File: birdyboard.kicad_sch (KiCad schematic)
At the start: 37 parts, among them J1 24V Input Screw Terminal, J10 JST-PH StepMotor Conn, J11 TBP02R2-381-04BE, J12 AS5047_Adapter_Board_Connector, J13 AS5047_Adapter_Board_Connector, J14 AS5047_Adapter_Board_Connector, J15 AS5047_Adapter_Board_Connector, J2 24V Input Screw Terminal, J3 24V Input Screw Terminal, J4 JST-PH StepMotor Conn, J5 JST-PH StepMotor Conn, J6 JST-PH StepMotor Conn, J7 TBP02R2-381-04BE, J8 TBP02R2-381-04BE, J9 TBP02R2-381-04BE, U3 Pico, U6 SN74CBT3253 MUX/DEMUX, U7 AZ1117CH-3_3TRG1

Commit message: Update Schematic Labels
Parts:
- gave numbers to parts that had none: 4
- renumbered J11 to J10, J10 to J3, U3 to U0, PS1 to U5, U7 to U6
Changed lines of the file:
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@@
   (symbol (lib_id "birdyboard_library:TMC2209_SILENTSTEPSTICK") (at 123.19 39.37 0) (unit 1)
     (in_bom yes) (on_board yes) (fields_autoplaced)
-    (property "Reference" "U?" (id 0) (at 110.49 20.32 0)
-      (effects (font (size 1.27 1.27)) (justify left bottom))
-    )
-    (property "Value" "TMC2209_SILENTSTEPSTICK" (id 1) (at 110.49 62.23 0)
-      (effects (font (size 1.27 1.27)) (justify left bottom))
-    )
+    (property "Reference" "U2" (id 0) (at 123.19 16.51 0))
+    (property "Value" "TMC2209_SILENTSTEPSTICK" (id 1) (at 123.19 19.05 0))
     (property "Footprint" "MODULE_TMC2208_SILENTSTEPSTICK" (id 2) (at 123.19 39.37 0)
       (effects (font (size 1.27 1.27)) (justify left bottom) hide)
@@
   (symbol (lib_id "birdyboard_library:TMC2209_SILENTSTEPSTICK") (at 43.815 172.085 0) (unit 1)
     (in_bom yes) (on_board yes) (fields_autoplaced)
-    (property "Reference" "U?" (id 0) (at 31.115 153.035 0)
-      (effects (font (size 1.27 1.27)) (justify left bottom))
-    )
-    (property "Value" "TMC2209_SILENTSTEPSTICK" (id 1) (at 31.115 194.945 0)
-      (effects (font (size 1.27 1.27)) (justify left bottom))
-    )
+    (property "Reference" "U3" (id 0) (at 43.815 148.59 0))
+    (property "Value" "TMC2209_SILENTSTEPSTICK" (id 1) (at 43.815 151.13 0))
     (property "Footprint" "MODULE_TMC2208_SILENTSTEPSTICK" (id 2) (at 43.815 172.085 0)
       (effects (font (size 1.27 1.27)) (justify left bottom) hide)
@@
   (symbol (lib_id "birdyboard_library:Pico") (at 102.87 106.68 0) (unit 1)
     (in_bom yes) (on_board yes) (fields_autoplaced)
-    (property "Reference" "U3" (id 0) (at 102.87 74.93 0))
+    (property "Reference" "U0" (id 0) (at 102.87 74.93 0))
     (property "Value" "Pico" (id 1) (at 102.87 77.47 0))
     (property "Footprint" "MCU_RaspberryPi_and_Boards:RPi_Pico_SMD_TH" (id 2) (at 102.87 106.68 90)
@@
   (symbol (lib_id "birdyboard_library:TBP02R2-381-04BE") (at 42.545 8.89 0) (unit 1)
     (in_bom yes) (on_board yes) (fields_autoplaced)
-    (property "Reference" "J11" (id 0) (at 49.53 6.3499 0)
+    (property "Reference" "J10" (id 0) (at 49.53 6.3499 0)
       (effects (font (size 1.27 1.27)) (justify left))
     )
@@
   (symbol (lib_id "birdyboard_library:K7805-3AR3") (at 202.565 60.96 0) (unit 1)
     (in_bom yes) (on_board yes) (fields_autoplaced)
-    (property "Reference" "PS1" (id 0) (at 202.565 45.72 0))
+    (property "Reference" "U5" (id 0) (at 202.565 45.72 0))
     (property "Value" "K7805-3AR3" (id 1) (at 202.565 48.26 0))
     (property "Footprint" "birdyboard:CONV_K7805-3AR3" (id 2) (at 202.565 50.8 0))
@@
   (symbol (lib_id "dk_PMIC-Voltage-Regulators-Linear:AZ1117CH-3_3TRG1") (at 201.93 24.765 0) (unit 1)
     (in_bom yes) (on_board yes) (fields_autoplaced)
-    (property "Reference" "U7" (id 0) (at 203.2 16.51 0)
+    (property "Reference" "U6" (id 0) (at 203.2 16.51 0)
       (effects (font (size 1.524 1.524)))
     )
@@
   (symbol (lib_id "Connector:Conn_01x04_Female") (at 163.195 171.45 0) (unit 1)
     (in_bom yes) (on_board yes)
-    (property "Reference" "J10" (id 0) (at 167.005 176.53 0)
+    (property "Reference" "J3" (id 0) (at 167.005 176.53 0)
       (effects (font (size 1.27 1.27)) (justify left))
     )
@@
   (symbol (lib_id "birdyboard_library:TMC2209_SILENTSTEPSTICK") (at 40.64 37.465 0) (unit 1)
     (in_bom yes) (on_board yes) (fields_autoplaced)
-    (property "Reference" "U?" (id 0) (at 27.94 18.415 0)
-      (effects (font (size 1.27 1.27)) (justify left bottom))
-    )
-    (property "Value" "TMC2209_SILENTSTEPSTICK" (id 1) (at 27.94 60.325 0)
-      (effects (font (size 1.27 1.27)) (justify left bottom))
-    )
+    (property "Reference" "U1" (id 0) (at 40.64 13.97 0))
+    (property "Value" "TMC2209_SILENTSTEPSTICK" (id 1) (at 40.64 16.51 0))
     (property "Footprint" "MODULE_TMC2208_SILENTSTEPSTICK" (id 2) (at 40.64 37.465 0)
       (effects (font (size 1.27 1.27)) (justify left bottom) hide)
@@
   (symbol (lib_id "birdyboard_library:TMC2209_SILENTSTEPSTICK") (at 132.715 171.45 0) (unit 1)
     (in_bom yes) (on_board yes) (fields_autoplaced)
-    (property "Reference" "U?" (id 0) (at 120.015 152.4 0)
-      (effects (font (size 1.27 1.27)) (justify left bottom))
-    )
-    (property "Value" "TMC2209_SILENTSTEPSTICK" (id 1) (at 120.015 194.31 0)
-      (effects (font (size 1.27 1.27)) (justify left bottom))
-    )
+    (property "Reference" "U4" (id 0) (at 132.715 148.59 0))
+    (property "Value" "TMC2209_SILENTSTEPSTICK" (id 1) (at 132.715 151.13 0))
     (property "Footprint" "MODULE_TMC2208_SILENTSTEPSTICK" (id 2) (at 132.715 171.45 0)
       (effects (font (size 1.27 1.27)) (justify left bottom) hide)
@@
       (reference "J2") (unit 1) (value "24V Input Screw Terminal") (footprint "birdyboard:CUI_TBP01R2-508-02BE")
     )
+    (path "/acf46d64-7022-46aa-a07f-964eb7e04114"
+      (reference "J3") (unit 1) (value "JST-PH StepMotor Conn") (footprint "Connector_JST:JST_XH_B4B-XH-A_1x04_P2.50mm_Vertical")
+    )
     (path "/f5df09cc-e7d8-40ed-81dc-431146d8ff35"
       (reference "J3") (unit 1) (value "24V Input Screw Terminal") (footprint "birdyboard:CUI_TBP01R2-508-02BE")
@@
       (reference "J9") (unit 1) (value "TBP02R2-381-04BE") (footprint "birdyboard:CUI_TBP02R2-381-04BE")
     )
-    (path "/acf46d64-7022-46aa-a07f-964eb7e04114"
-      (reference "J10") (unit 1) (value "JST-PH StepMotor Conn") (footprint "Connector_JST:JST_XH_B4B-XH-A_1x04_P2.50mm_Vertical")
-    )
     (path "/6c972ed1-f9ff-48f3-b910-a3798639139c"
-      (reference "J11") (unit 1) (value "TBP02R2-381-04BE") (footprint "birdyboard:CUI_TBP02R2-381-04BE")
+      (reference "J10") (unit 1) (value "TBP02R2-381-04BE") (footprint "birdyboard:CUI_TBP02R2-381-04BE")
     )
     (path "/3bced514-7c6a-4929-a2f4-97c9dfd34def"
@@
       (reference "JP?") (unit 1) (value "SolderJumper_3_Bridged12") (footprint "")
     )
-    (path "/8ce54405-acb6-4808-8ae9-05b938524726"
-      (reference "PS1") (unit 1) (value "K7805-3AR3") (footprint "birdyboard:CONV_K7805-3AR3")
-    )
     (path "/1383c2e0-9014-4320-87a3-9259c9c126ad"
       (reference "R?") (unit 1) (value "R") (footprint "")
@@
     )
     (path "/5c28b9b9-20a8-48b6-ba53-d717d342083f"
-      (reference "U3") (unit 1) (value "Pico") (footprint "MCU_RaspberryPi_and_Boards:RPi_Pico_SMD_TH")
+      (reference "U0") (unit 1) (value "Pico") (footprint "MCU_RaspberryPi_and_Boards:RPi_Pico_SMD_TH")
+    )
+    (path "/c5ba89e5-abf6-44af-8c5f-769135662d59"
+      (reference "U1") (unit 1) (value "TMC2209_SILENTSTEPSTICK") (footprint "MODULE_TMC2208_SILENTSTEPSTICK")
+    )
+    (path "/1b7241dd-50c0-4ea4-b9e4-398fecb92930"
+      (reference "U2") (unit 1) (value "TMC2209_SILENTSTEPSTICK") (footprint "MODULE_TMC2208_SILENTSTEPSTICK")
+    )
+    (path "/344822b8-0c78-4832-98d5-254b8b20341d"
+      (reference "U3") (unit 1) (value "TMC2209_SILENTSTEPSTICK") (footprint "MODULE_TMC2208_SILENTSTEPSTICK")
+    )
+    (path "/f64ad3d7-b9b7-403e-af6d-671c637d8a55"
+      (reference "U4") (unit 1) (value "TMC2209_SILENTSTEPSTICK") (footprint "MODULE_TMC2208_SILENTSTEPSTICK")
+    )
+    (path "/8ce54405-acb6-4808-8ae9-05b938524726"
+      (reference "U5") (unit 1) (value "K7805-3AR3") (footprint "birdyboard:CONV_K7805-3AR3")
     )
     (path "/71a1570f-8306-437b-8e8c-580fc1ad37d6"
@@
     )
     (path "/a15739ab-9211-4aeb-9603-bc7b827421d7"
-      (reference "U7") (unit 1) (value "AZ1117CH-3_3TRG1") (footprint "digikey-footprints:SOT-223")
-    )
-    (path "/1b7241dd-50c0-4ea4-b9e4-398fecb92930"
-      (reference "U?") (unit 1) (value "TMC2209_SILENTSTEPSTICK") (footprint "MODULE_TMC2208_SILENTSTEPSTICK")
-    )
-    (path "/344822b8-0c78-4832-98d5-254b8b20341d"
-      (reference "U?") (unit 1) (value "TMC2209_SILENTSTEPSTICK") (footprint "MODULE_TMC2208_SILENTSTEPSTICK")
-    )
-    (path "/c5ba89e5-abf6-44af-8c5f-769135662d59"
-      (reference "U?") (unit 1) (value "TMC2209_SILENTSTEPSTICK") (footprint "MODULE_TMC2208_SILENTSTEPSTICK")
-    )
-    (path "/f64ad3d7-b9b7-403e-af6d-671c637d8a55"
-      (reference "U?") (unit 1) (value "TMC2209_SILENTSTEPSTICK") (footprint "MODULE_TMC2208_SILENTSTEPSTICK")
-    )
-  )
+      (reference "U6") (unit 1) (value "AZ1117CH-3_3TRG1") (footprint "digikey-footprints:SOT-223")
+    )
+  )

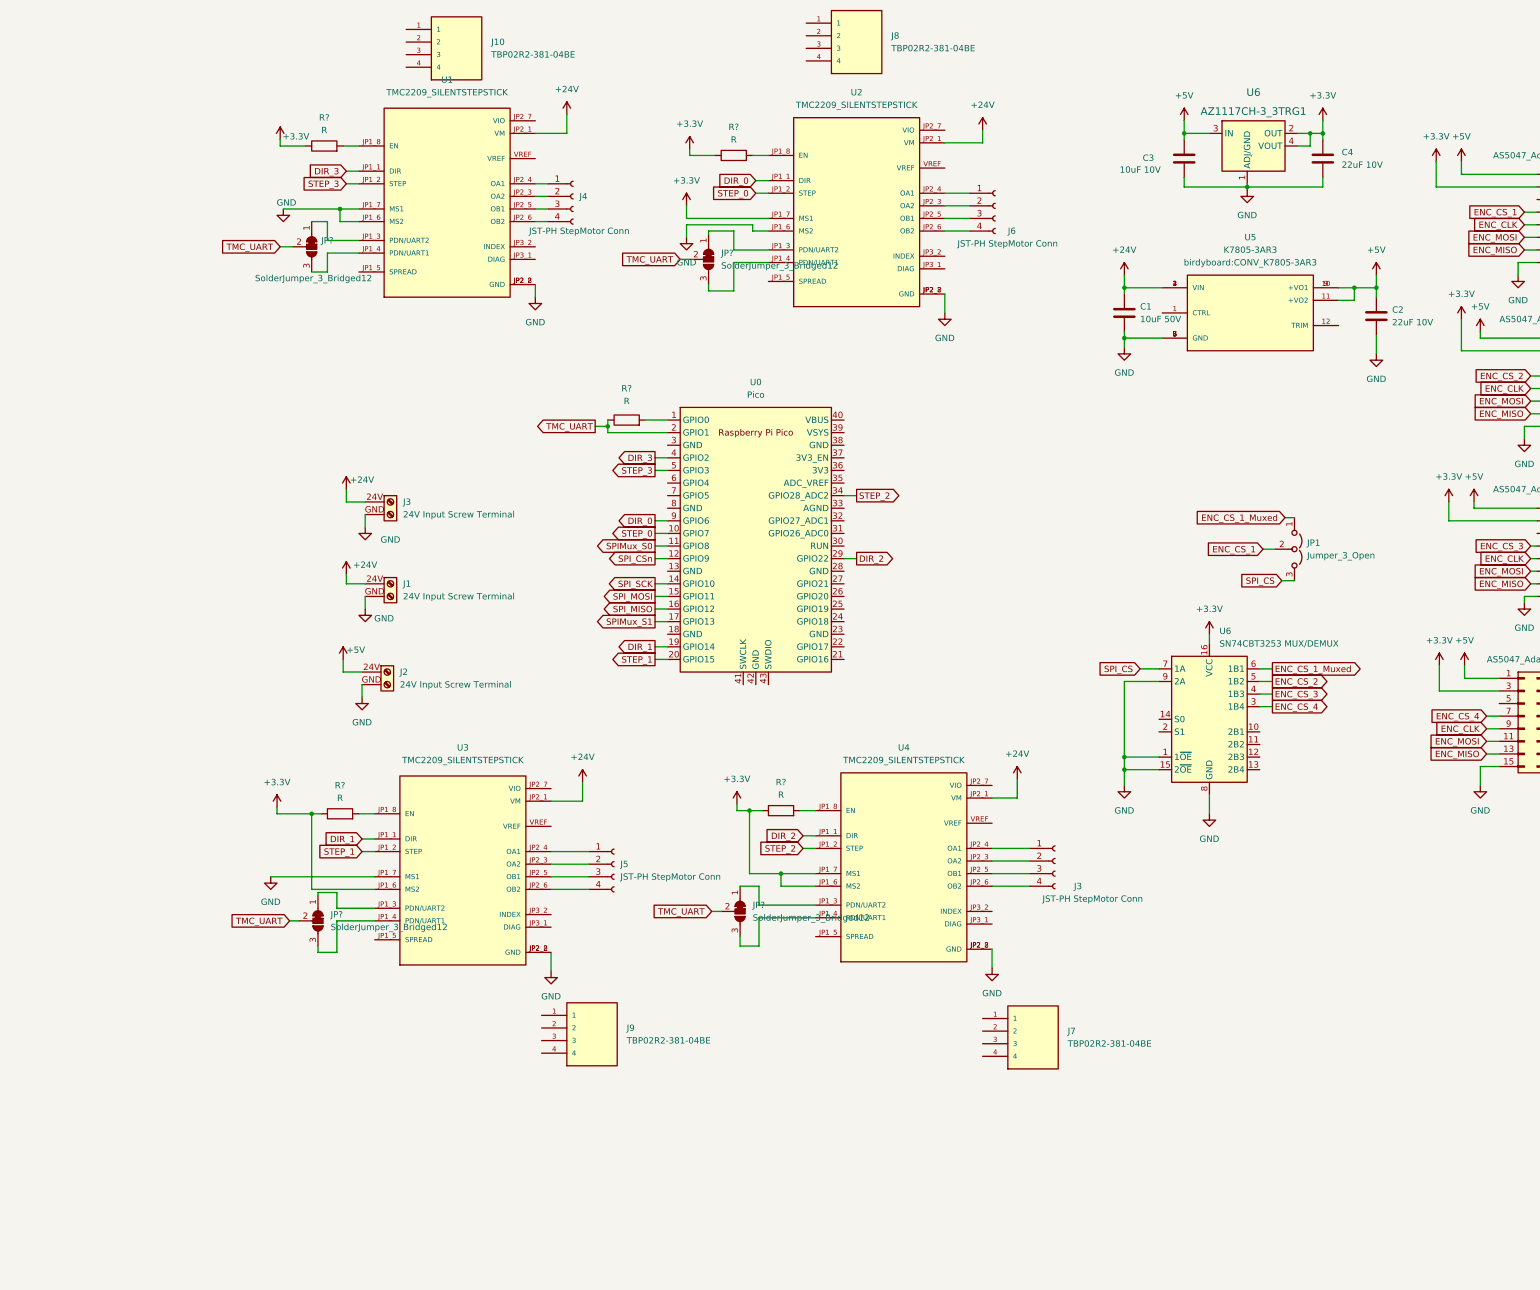
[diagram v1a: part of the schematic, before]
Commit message: Adds 40-pin header, cleans up stepper connections, add VIO connections for TMC, hooks up RP-PICO Power
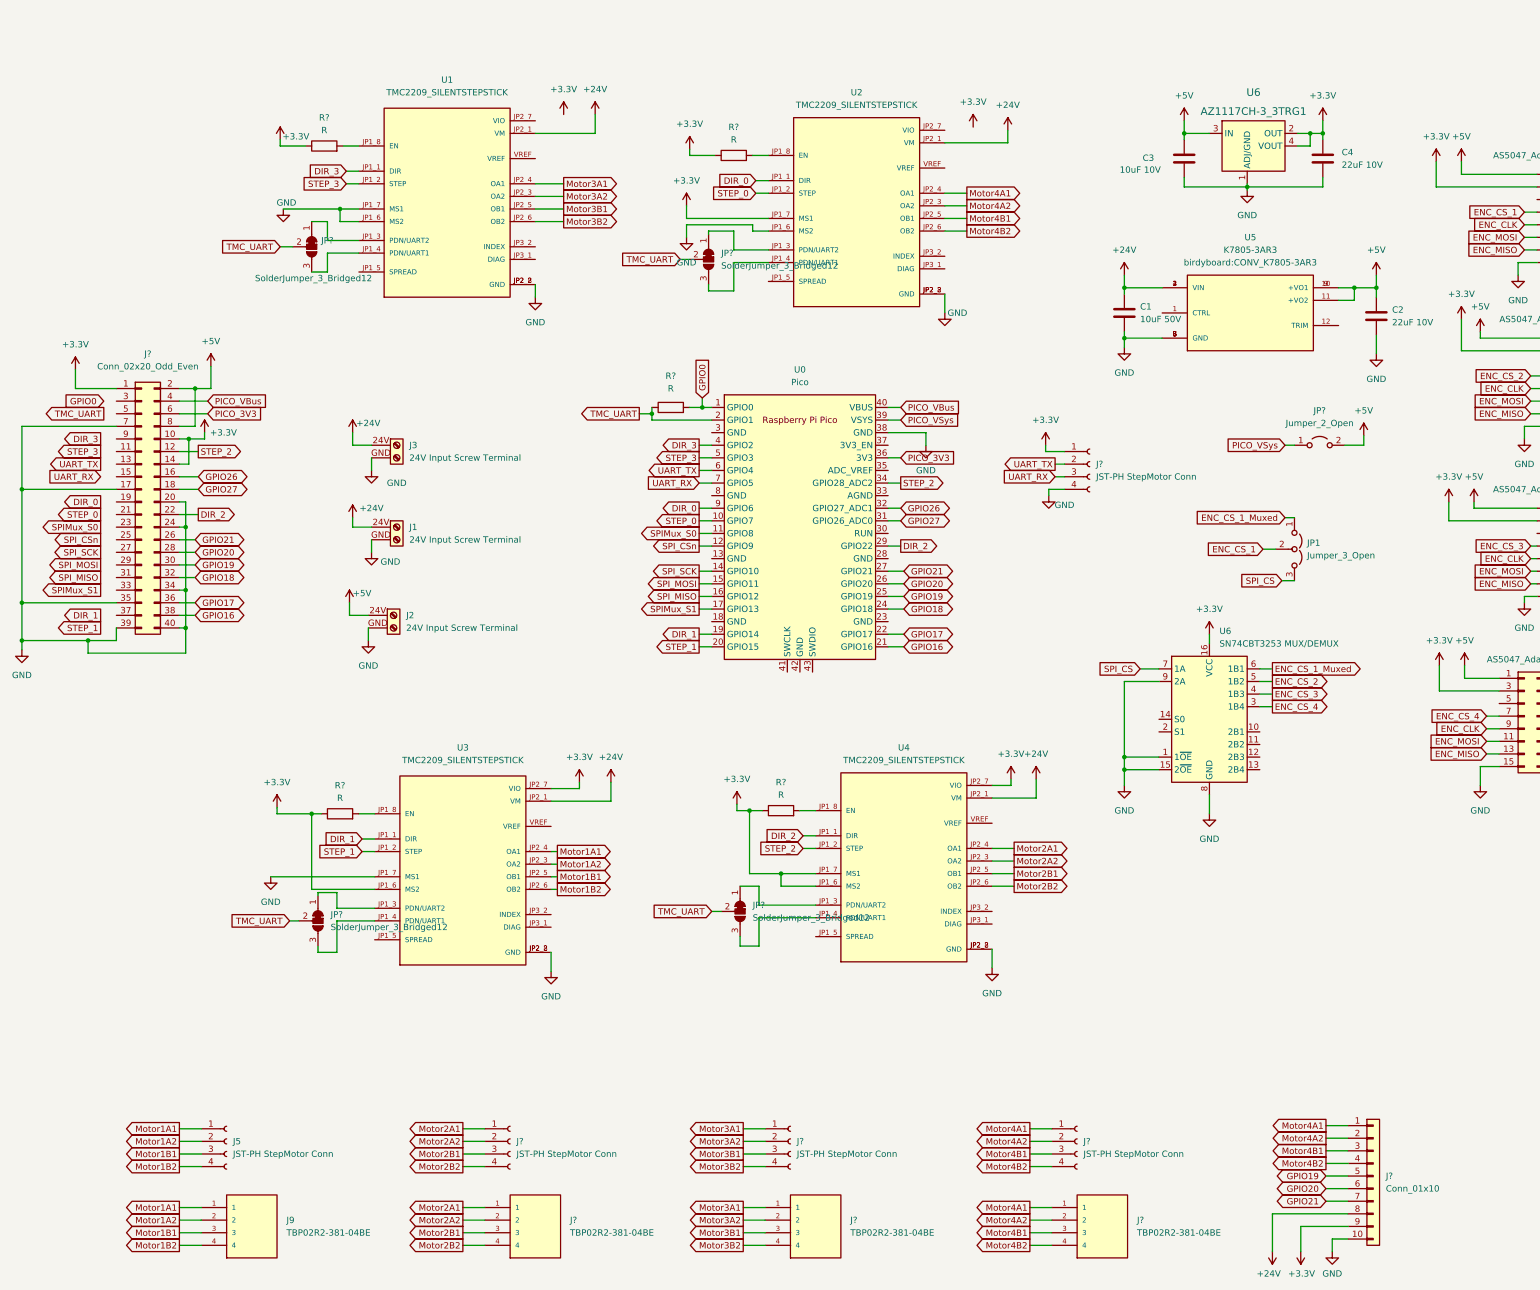
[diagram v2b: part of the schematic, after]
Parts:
- removed J10, J7, J8: TBP02R2-381-04BE, birdyboard:CUI_TBP02R2-381-04BE, symbol birdyboard_library:TBP02R2-381-04BE
- removed J3, J4, J6: JST-PH StepMotor Conn, Connector_JST:JST_XH_B4B-XH-A_1x04_P2.50mm_Vertical, symbol Connector:Conn_01x04_Female
- added J? (x4): JST-PH StepMotor Conn, Connector_JST:JST_XH_B4B-XH-A_1x04_P2.50mm_Vertical, symbol Connector:Conn_01x04_Female
- added J? (x3): TBP02R2-381-04BE, birdyboard:CUI_TBP02R2-381-04BE, symbol birdyboard_library:TBP02R2-381-04BE
- added J?: Conn_02x20_Odd_Even, Connector_PinHeader_2.54mm:PinHeader_2x20_P2.54mm_Vertical, symbol Connector_Generic:Conn_02x20_Odd_Even
- added J?: Conn_01x10, symbol Connector_Generic:Conn_01x10
- added JP?: Jumper_2_Open, symbol Jumper:Jumper_2_Open
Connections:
- net +24V: now also J?.8 (Pin_8)
- net +3.3V: now also J?.1 (Pin_1), J?.1 (Pin_1), J?.10 (Pin_10), J?.14 (Pin_14), J?.9 (Pin_9)
- net +3V3: now also U3.JP2_7 (VIO), U4.JP2_7 (VIO)
- net +5V: now also J?.2 (Pin_2), J?.8 (Pin_8), JP?.2 (B)
- net DIR_2: now also J?.22 (Pin_22)
- net GND: now also U0.38 (GND), J?.10 (Pin_10), J?.17 (Pin_17), J?.20 (Pin_20), J?.24 (Pin_24), J?.34 (Pin_34), J?.35 (Pin_35), J?.39 (Pin_39), J?.4 (Pin_4), J?.40 (Pin_40), J?.7 (Pin_7)
- net STEP_2: now also J?.12 (Pin_12)
- net GPIO0: now reaches R?.2, U0.1 (GPIO0)
- net Motor4A2: now reaches U2.JP2_3 (OA2)
- net Motor4A2: now also J?.2, J?.2 (Pin_2), J?.2 (Pin_2)
- net Motor4A1: now reaches U2.JP2_4 (OA1)
- net Motor4A1: now also J?.1, J?.1 (Pin_1), J?.1 (Pin_1)
- net Motor4B1: now reaches U2.JP2_5 (OB1)
- net Motor4B1: now also J?.3, J?.3 (Pin_3), J?.3 (Pin_3)
- net Motor4B2: now reaches U2.JP2_6 (OB2)
- net Motor4B2: now also J?.4, J?.4 (Pin_4), J?.4 (Pin_4)
- net Motor1A2: now reaches J5.2 (Pin_2), U3.JP2_3 (OA2)
- net Motor1A2: now also J9.2
- net Motor1A1: now reaches J5.1 (Pin_1), U3.JP2_4 (OA1)
- net Motor1A1: now also J9.1
- net Motor1B1: now reaches J5.3 (Pin_3), U3.JP2_5 (OB1)
- net Motor1B1: now also J9.3
- net Motor1B2: now reaches J5.4 (Pin_4), U3.JP2_6 (OB2)
- net Motor1B2: now also J9.4
- net GPIO16: now reaches U0.21 (GPIO16)
- net GPIO16: now also J?.38 (Pin_38)
- net GPIO17: now reaches U0.22 (GPIO17)
- net GPIO17: now also J?.36 (Pin_36)
- net GPIO18: now reaches U0.24 (GPIO18)
- net GPIO18: now also J?.32 (Pin_32)
- net GPIO19: now reaches U0.25 (GPIO19)
- net GPIO19: now also J?.30 (Pin_30), J?.5 (Pin_5)
- net GPIO20: now reaches U0.26 (GPIO20)
- net GPIO20: now also J?.28 (Pin_28), J?.6 (Pin_6)
- net GPIO21: now reaches U0.27 (GPIO21)
- net GPIO21: now also J?.26 (Pin_26), J?.7 (Pin_7)
- net GPIO27: now reaches U0.31 (GPIO26_ADC0)
- net GPIO27: now also J?.18 (Pin_18)
- net GPIO26: now reaches U0.32 (GPIO27_ADC1)
- net GPIO26: now also J?.16 (Pin_16)
- net PICO_3V3: now reaches U0.36 (3V3)
- net PICO_3V3: now also J?.6 (Pin_6)
- net PICO_VSys: now reaches U0.39 (VSYS)
- net PICO_VSys: now also JP?.1 (A)
- net PICO_VBus: now reaches U0.40 (VBUS)
- net PICO_VBus: now also J?.4 (Pin_4)
- net UART_TX: now reaches U0.6 (GPIO4)
- net UART_TX: now also J?.2 (Pin_2)
- net UART_RX: now reaches U0.7 (GPIO5)
- net UART_RX: now also J?.3 (Pin_3)
- net Motor3A1: now reaches U1.JP2_4 (OA1)
- net Motor3A1: now also J?.1, J?.1 (Pin_1)
- net Motor3A2: now reaches U1.JP2_3 (OA2)
- net Motor3A2: now also J?.2, J?.2 (Pin_2)
- net Motor3B1: now reaches U1.JP2_5 (OB1)
- net Motor3B1: now also J?.3, J?.3 (Pin_3)
- net Motor3B2: now reaches U1.JP2_6 (OB2)
- net Motor3B2: now also J?.4, J?.4 (Pin_4)
- net Motor2A1: now reaches U4.JP2_4 (OA1)
- net Motor2A1: now also J?.1, J?.1 (Pin_1)
- net Motor2A2: now reaches U4.JP2_3 (OA2)
- net Motor2A2: now also J?.2, J?.2 (Pin_2)
- net Motor2B1: now reaches U4.JP2_5 (OB1)
- net Motor2B1: now also J?.3, J?.3 (Pin_3)
- net Motor2B2: now reaches U4.JP2_6 (OB2)
- net Motor2B2: now also J?.4, J?.4 (Pin_4)
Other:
- moved on the sheet: J1, J2, J3, J5, J9, R?, U0
